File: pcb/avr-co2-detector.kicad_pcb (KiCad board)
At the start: 2 copper layers, 100 x 70 mm, 70 parts, among them J1 USB TYPE-C, J2 Backlight, J3 Backlight, J4 LCD0802, J5 AVR-ISP-10, J6 BH1.27-6-2, SW1 "Reset", SW2 "Reset", U1 ATtiny2313A-SU, U2 FT232RL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

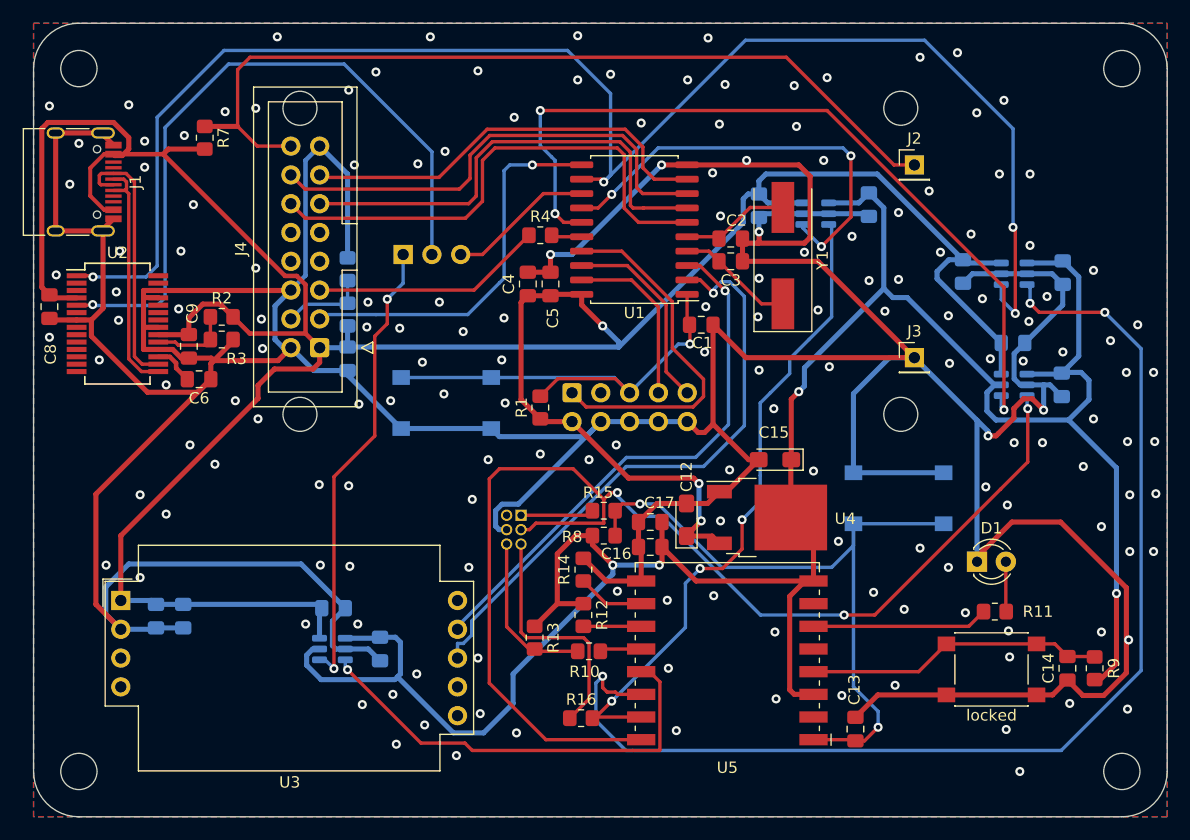
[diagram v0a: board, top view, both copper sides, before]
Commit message: Fixed LCD connector pinout, corrected resistor R16 connection
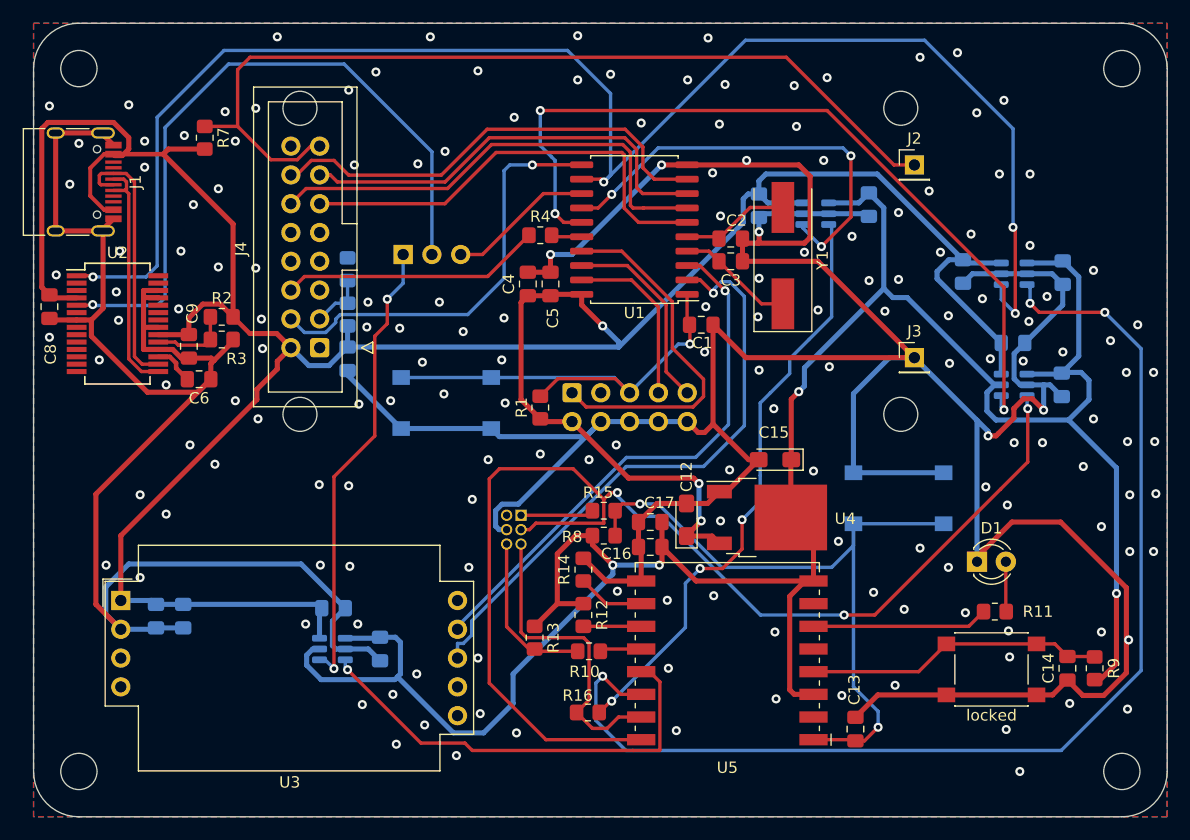
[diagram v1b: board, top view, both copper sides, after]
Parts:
- moved R16 0.78 mm to (131.9, 124.8)
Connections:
- J4 pad 1: +5V -> GND
- J4 pad 11: /DB5 -> /DB4
- J4 pad 12: /DB4 -> /DB5
- J4 pad 13: /DB7 -> /DB6
- J4 pad 14: /DB6 -> /DB7
- J4 pad 15: GND -> /LED+
- J4 pad 16: /LED+ -> GND
- J4 pad 2: GND -> +5V
- J4 pad 3: /RS -> /VO
- J4 pad 4: /VO -> /RS
- J4 pad 5: /E -> GND
- J4 pad 6: GND -> /E
- U5 pad 15: Net-(R16-Pad2) -> /ESP_RXD
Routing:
- net GND: track 503.8 -> 447.7 mm, vias 168 -> 171
- net +5V: track 275.3 -> 268.8 mm
- net /DB4: track 45.6 -> 39.6 mm
- net /ESP_RXD: track 21.5 -> 27.4 mm
- net Net-(R16-Pad2): track 58.0 -> 52.9 mm
- net /DB6: track 42.7 -> 38.3 mm
- net /RS: track 34.3 -> 38.0 mm
- net /LED+: track 77.4 -> 80.9 mm
- net /DB7: track 37.2 -> 40.6 mm
- net /VO: track 7.57 -> 5.03 mm
- net /E: track 20.5 -> 23.0 mm
- net /ESP_DEBUG_RXD: track 102.5 -> 101.9 mm

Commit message: Increased width of traces of 3.3V and 5V, mirrored project info on silkscreen, added "Debug UART" connector
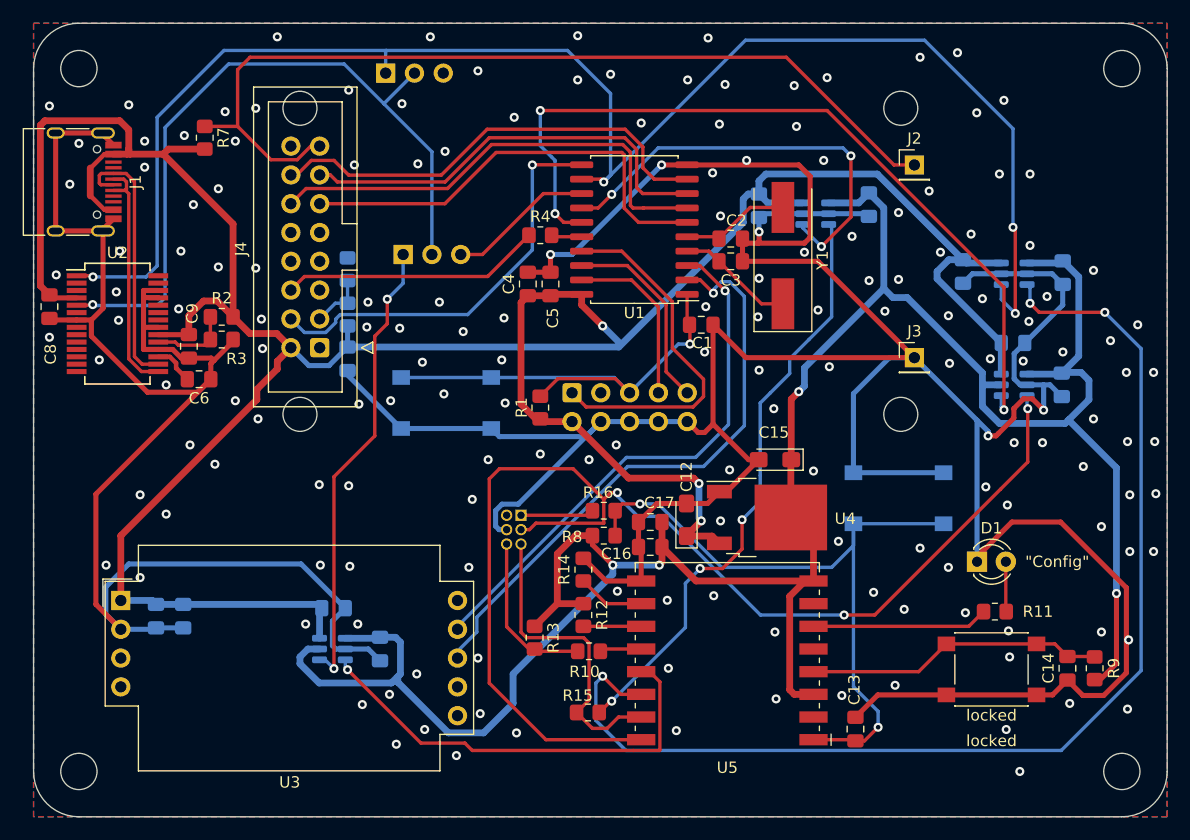
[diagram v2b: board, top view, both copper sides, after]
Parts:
- added J6: "Debug UART", Connector_PinHeader_2.54mm:PinHeader_1x03_P2.54mm_Vertical, B.Cu at (114.1, 68.4)
- J7: renamed from J6; value BH1.27-6-2 -> "ESP-Prog"
- SW1: value "Reset" -> "Reset AVR"
- SW2: value "Reset" -> "Reset ESP"
- renumbered R16 to R15, R15 to R16
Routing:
- net Net-(J6-Pad2): track 61.3 -> 65.1 mm
- net +3.3V: track 217.9 -> 220.2 mm
- net /AVR_DEBUG_RXD: track 138.7 -> 140.7 mm
- net /RS: track 38.0 -> 36.8 mm
- net +5V: track 268.8 -> 269.4 mm

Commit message: Added GND TestPoint, assigned revision 2, updated Gerber and drill files
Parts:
- added TP1: GND TestPoint, TestPoint:TestPoint_Bridge_Pitch2.54mm_Drill1.0mm, F.Cu at (174.8, 77.3)
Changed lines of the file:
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@@
   (title_block
     (title "AVR CO2 detector")
-    (date "2024-04-13")
-    (rev "rev. 1")
+    (date "2024-04-25")
+    (rev "rev.2")
     (company "antiQuery")
   )
@@
     )
   )
+  (footprint "TestPoint:TestPoint_Bridge_Pitch2.54mm_Drill1.0mm" (layer "F.Cu")
+    (at 174.8 77.3)
+    (descr "wire loop as test point, pitch 2.54mm, hole diameter 1.0mm, wire diameter 0.8mm")
+    (tags "test point wire loop")
+    (property "Sheetfile" "avr-co2-detector.kicad_sch")
+    (property "Sheetname" "")
+    (attr through_hole)
+    (fp_text reference "TP1" (at 1.1 2.1) (layer "F.SilkS")
+      (effects (font (size 1 1) (thickness 0.15)))
+    )
+    (fp_text value "GND TestPoint" (at 1 -1.7) (layer "F.Fab")
+      (effects (font (size 1 1) (thickness 0.15)))
+    )
+    (fp_text user "${REFERENCE}" (at 1.1 2.1) (layer "F.Fab")
+      (effects (font (size 1 1) (thickness 0.15)))
+    )
+    (fp_line (start 3.7 -1.2) (end -1.2 -1.2) (layer "F.SilkS") (width 0.12))
+    (fp_line (start -1.2 1.2) (end 3.7 1.2) (layer "F.SilkS") (width 0.12))
+    (fp_line (start 3.7 1.2) (end 3.7 -1.2) (layer "F.SilkS") (width 0.12))
+    (fp_line (start -1.2 -1.2) (end -1.2 1.2) (layer "F.SilkS") (width 0.12))
+    (fp_line (start -1.5 -1.5) (end -1.5 1.5) (layer "F.CrtYd") (width 0.05))
+    (fp_line (start 4.04 1.5) (end 4.04 -1.5) (layer "F.CrtYd") (width 0.05))
+    (fp_line (start 4.04 1.5) (end -1.5 1.5) (layer "F.CrtYd") (width 0.05))
+    (fp_line (start -1.5 -1.5) (end 4.04 -1.5) (layer "F.CrtYd") (width 0.05))
+    (fp_line (start 2.54 0) (end 0 0) (layer "F.Fab") (width 0.12))
+    (pad "1" thru_hole circle (at 0 0) (size 2 2) (drill 1) (layers *.Cu *.Mask)
+      (net 1 "GND") (pinfunction "1") (pintype "passive"))
+    (pad "1" thru_hole circle (at 2.54 0) (size 2 2) (drill 1) (layers *.Cu *.Mask)
+      (net 1 "GND") (pinfunction "1") (pintype "passive"))
+    (model "${KICAD6_3DMODEL_DIR}/TestPoint.3dshapes/TestPoint_Bridge_Pitch2.54mm_Drill1.0mm.wrl"
+      (offset (xyz 0 0 0))
+      (scale (xyz 1 1 1))
+      (rotate (xyz 0 0 0))
+    )
+  )
   (footprint "Resistor_SMD:R_0805_2012Metric_Pad1.20x1.40mm_HandSolder" (layer "F.Cu")
     (at 133.3 109.2)
@@
     (effects (font (size 1.5 1.5) (thickness 0.3)) (justify mirror))
   )
+  (gr_text "${TITLE}\n${REVISION}\n© ${ISSUE_DATE} ${COMPANY}" (at 106.2 105.1) (layer "F.SilkS")
+    (effects (font (size 1.5 1.5) (thickness 0.3)))
+  )
   (dimension (type aligned) (layer "F.Fab")
